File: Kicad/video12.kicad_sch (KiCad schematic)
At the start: 18 parts, among them J401 DE15HD, U401 THS7316, U402 TPD7S019

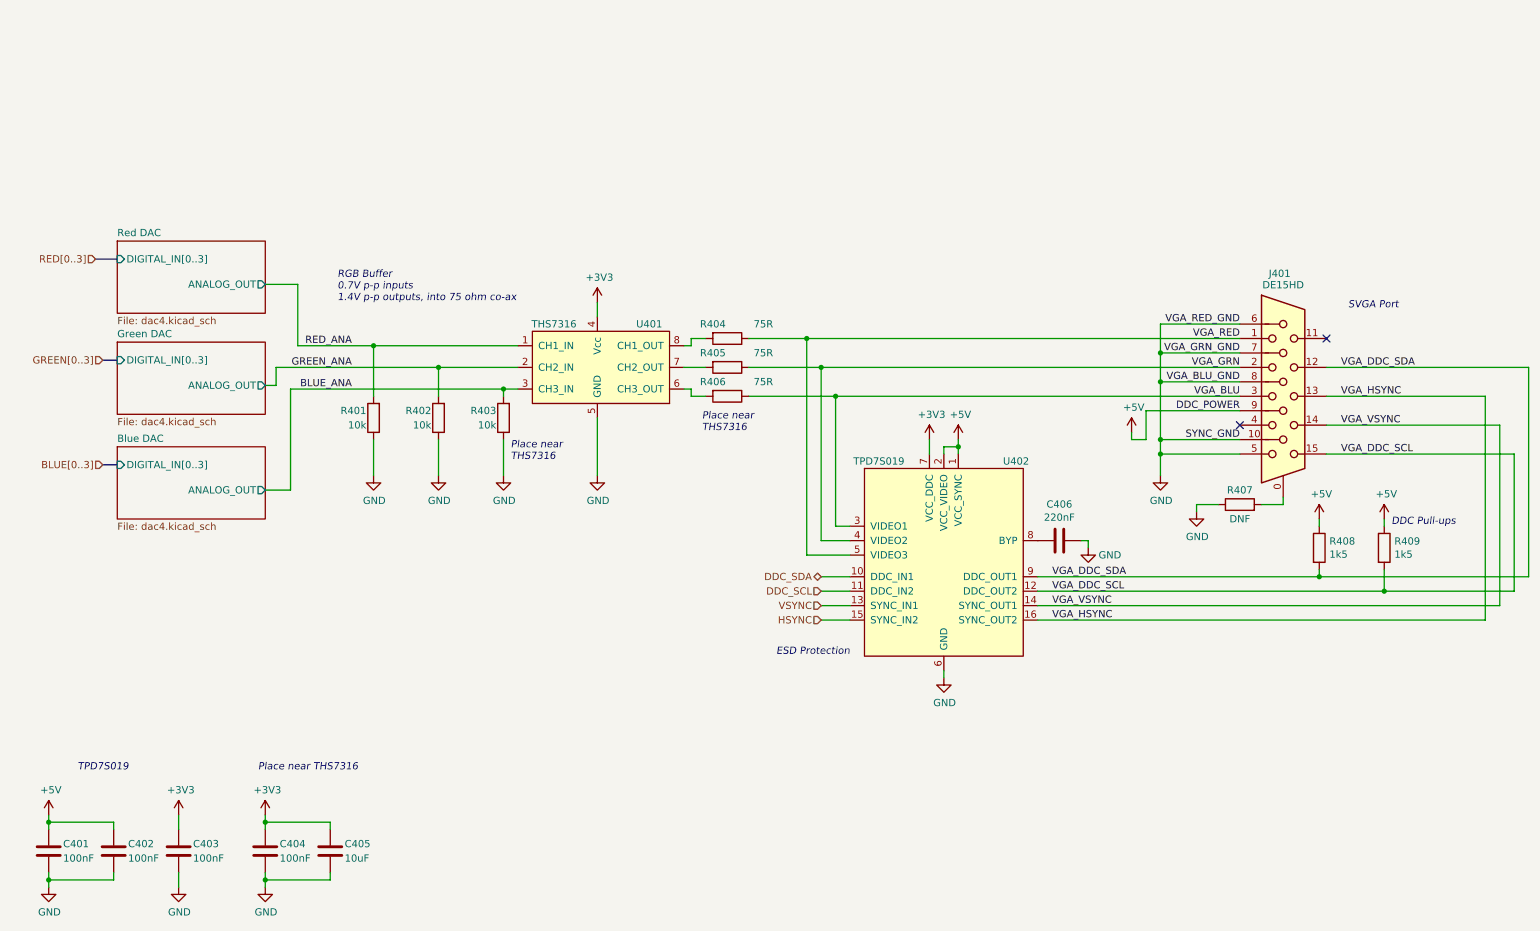
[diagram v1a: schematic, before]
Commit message: Retitle sheets and renumber parts.
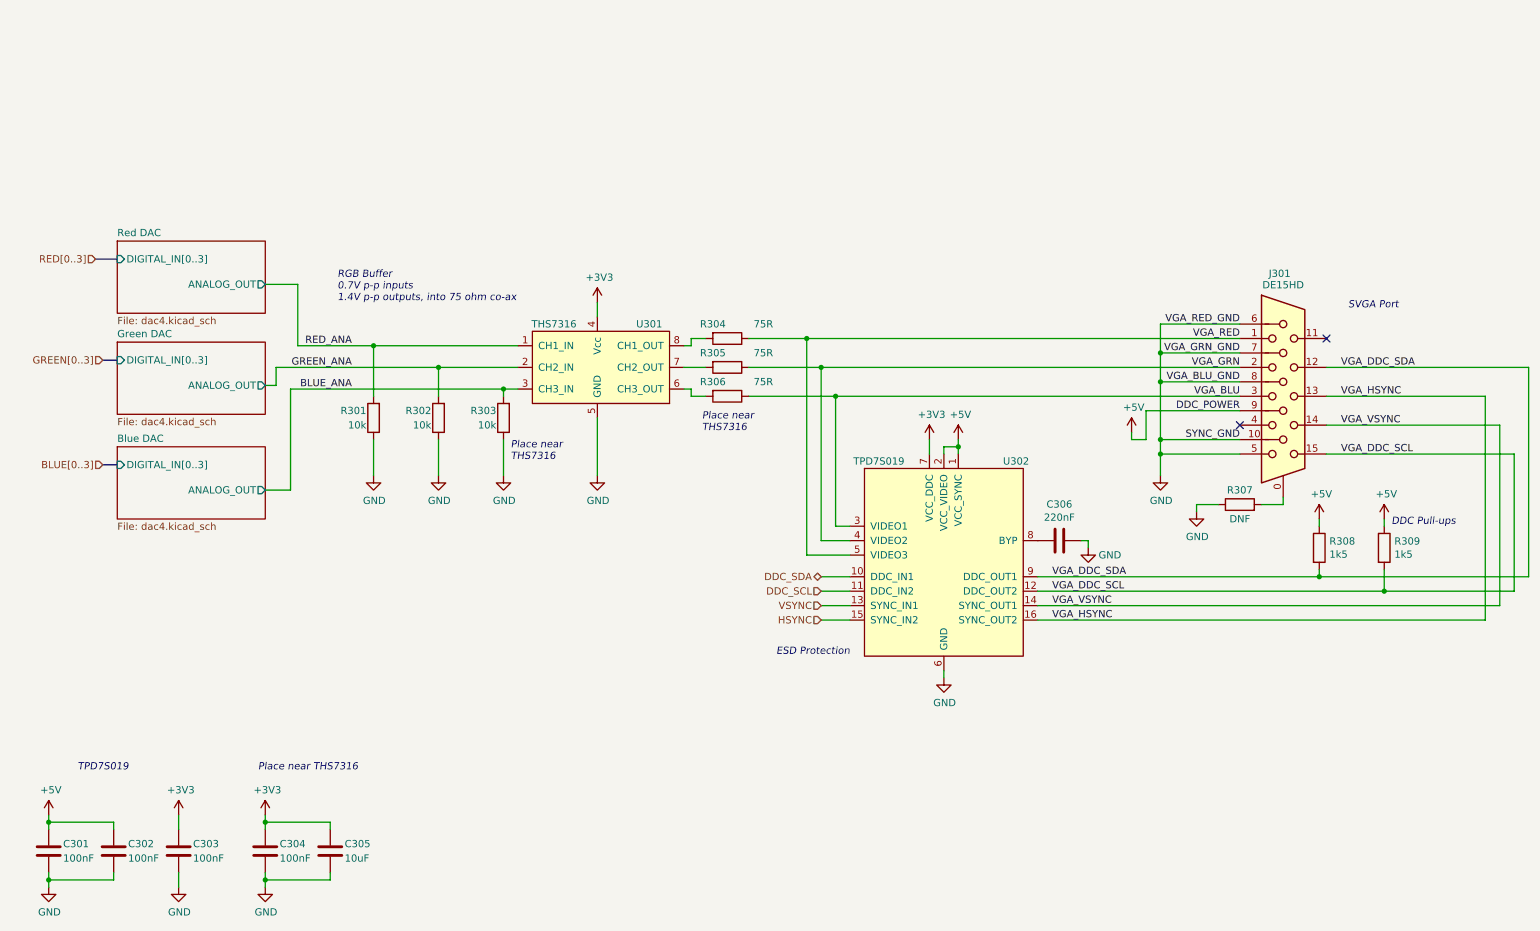
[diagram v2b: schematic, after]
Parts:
- renumbered C401 to C301, C402 to C302, C403 to C303, C404 to C304, C405 to C305, C406 to C306, J401 to J301, R401 to R301, R402 to R302, R403 to R303, R404 to R304, R405 to R305, R406 to R306, R407 to R307, R408 to R308, R409 to R309, U401 to U301, U402 to U302
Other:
- company: https://neotron-compute.github.io/ -> https://neotron-compute.github.io

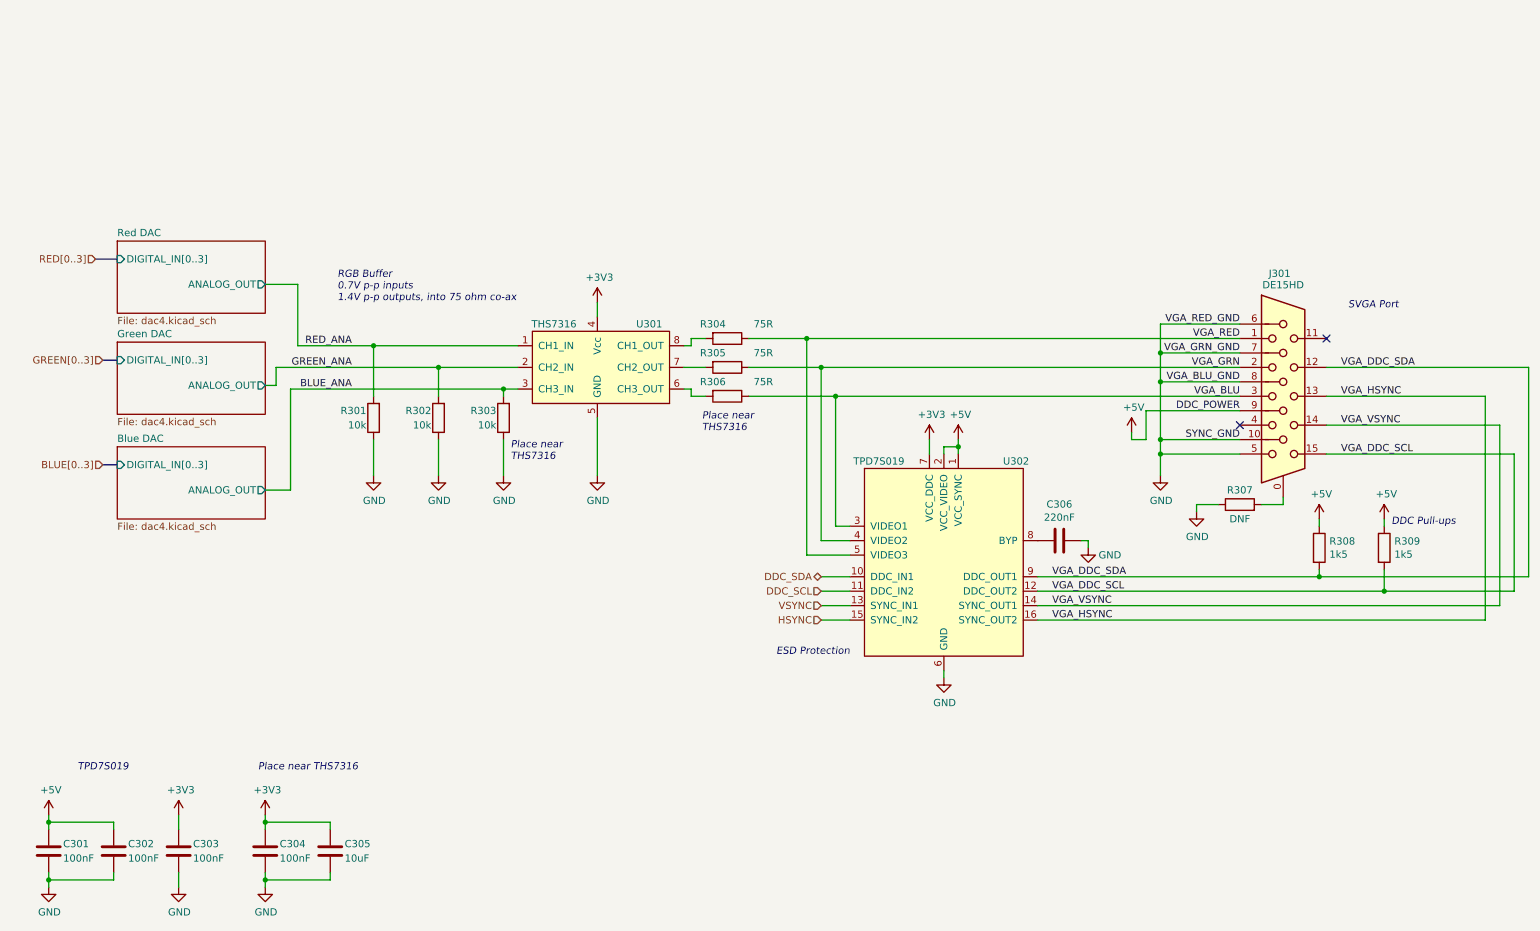
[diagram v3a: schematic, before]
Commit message: Set DAC to 1k/2k. Closes #77 Replaced some CPL resistors. Partial fix for #83 Added bridges for VGA I2C if ESD chip not fitted. Closes #51
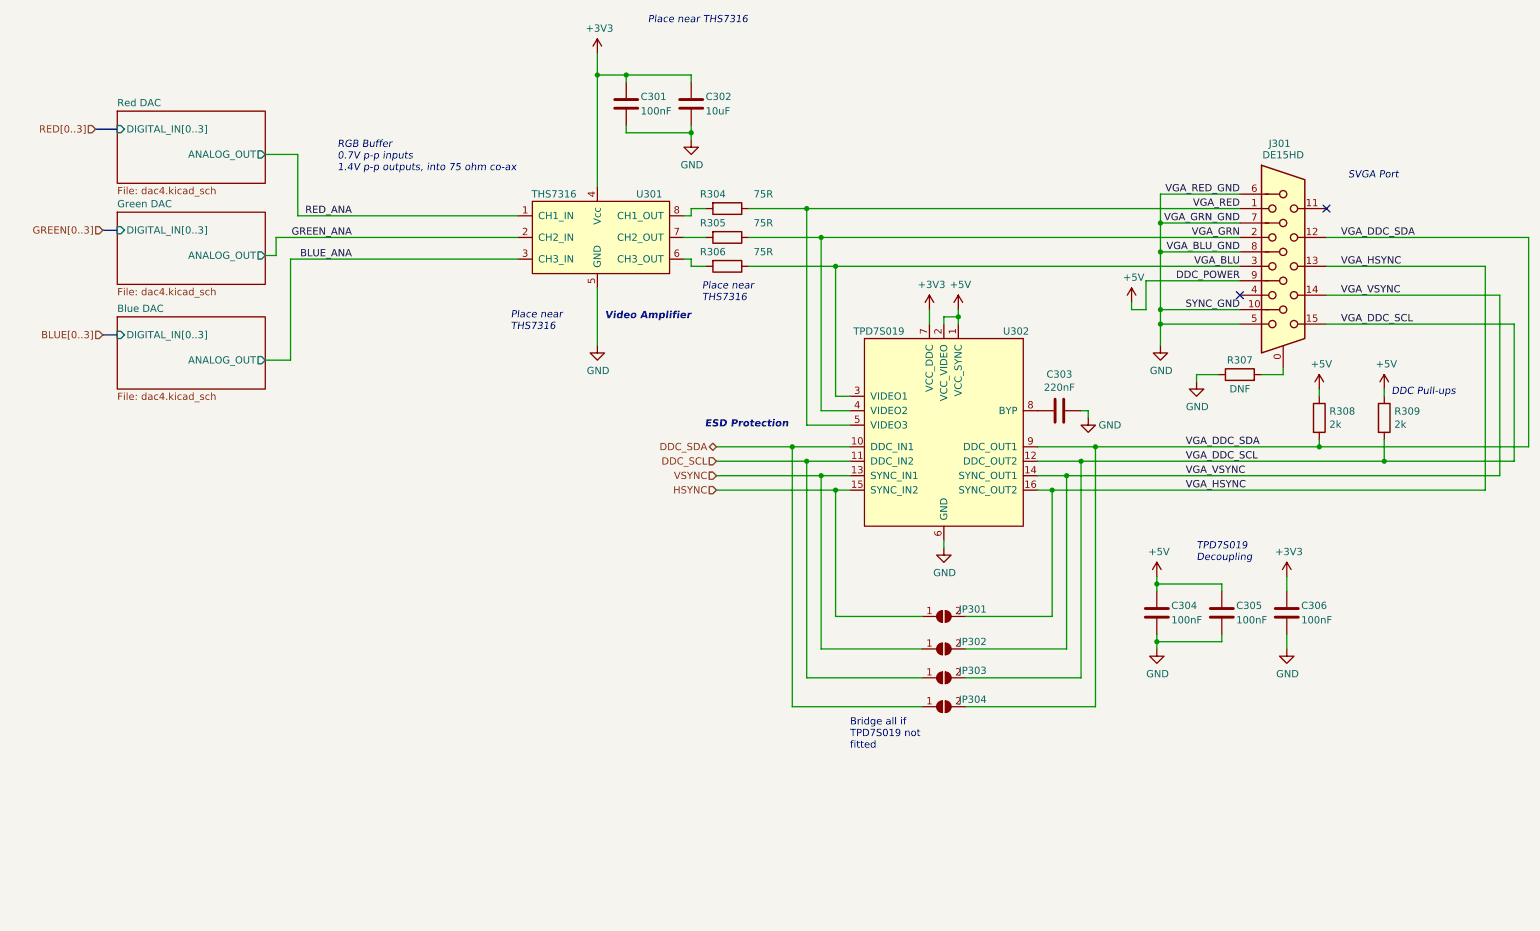
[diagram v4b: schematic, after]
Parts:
- removed R301, R302, R303: 10k, Resistor_SMD:R_0805_2012Metric_Pad1.20x1.40mm_HandSolder, symbol Device:R
- added JP301, JP302, JP303, JP304: Bridge, Jumper:SolderJumper-2_P1.3mm_Open_RoundedPad1.0x1.5mm, symbol Jumper:SolderJumper_2_Open
- R304, R305, R306: Digikey RMCF0805FT75R0-ND -> RMCF0805FT75R0CT-ND
- R308, R309: value 1k5 -> 2k; Digikey RMCF0805FT1K50-ND -> RMCF0805FT2K00CT-ND; LCSC Part# C4310 -> C17604; MPN RMCF0805FT1K50 -> RMCF0805FT2K00
- renumbered C304 to C301, C305 to C302, C306 to C303, C301 to C304, C302 to C305, C303 to C306
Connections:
- net DDC_SCL: now also JP303.1 (A)
- net DDC_SDA: now also JP304.1 (A)
- net HSYNC: now also JP301.1 (A)
- net VGA_DDC_SCL: now also JP303.2 (B)
- net VGA_DDC_SDA: now also JP304.2 (B)
- net VGA_HSYNC: now also JP301.2 (B)
- net VGA_VSYNC: now also JP302.2 (B)
- net VSYNC: now also JP302.1 (A)
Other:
- note added: "Bridge all if TPD7S019 not fitted"
- note added: "TPD7S019 Decoupling"
- note added: "Video Amplifier"
- note removed: "TPD7S019"
- moved on the sheet: C301, C302, C303, C304, C305, C306, J301, R304, R305, R306, R307, R308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

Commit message: Removed all CPL parts, and changed standby PSU.
The Holtek was a SOT-89 that had a completely different pinout to
every other SOT-89 3.3V LDO out there. To avoid confusion I
wanted to replace it, but the only other basic JLCPCB parts
were the AMS1117 (huge quiescent current) and something only
rated to 7V input voltage (this LDO gets the full VDC in).

So, I used a TO-92 footprint and picked an LP2950N.

This, however, needs some ESR on the output cap, so I made
that a 2.2uF electrolytic.

I also removed the 2x 10uF output caps on the K7805 and set
just one 22uF as specified in the datasheet.
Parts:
- C301, C304, C305, C306: Digikey (none) -> 399-C0805C104M5RAC7800CT-ND; MPN CPL-CAP-X7R-0805-100NF-50V -> C0805C104M5RACTU; Manufacturer CPL -> Kemet; Mouser (none) -> 80-C0805C104M5R
- C302: Digikey (none) -> 490-3886-1-ND; MPN CPL-CAP-X5R-0805-10UF-16V -> GRM21BR61C106KE15L; Manufacturer CPL -> Murata; Mouser (none) -> 81-GRM21BR61C106KE15
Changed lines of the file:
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@@
       (effects (font (size 1.27 1.27)) hide)
     )
-    (property "Digikey" "~" (id 5) (at 226.695 139.7 0)
-      (effects (font (size 1.27 1.27)) hide)
-    )
-    (property "MPN" "CPL-CAP-X7R-0805-100NF-50V" (id 6) (at 226.695 139.7 0)
-      (effects (font (size 1.27 1.27)) hide)
-    )
-    (property "Manufacturer" "CPL" (id 7) (at 226.695 139.7 0)
-      (effects (font (size 1.27 1.27)) hide)
-    )
-    (property "Mouser" "~" (id 8) (at 226.695 139.7 0)
+    (property "Digikey" "399-C0805C104M5RAC7800CT-ND" (id 5) (at 226.695 139.7 0)
+      (effects (font (size 1.27 1.27)) hide)
+    )
+    (property "MPN" "C0805C104M5RACTU" (id 6) (at 226.695 139.7 0)
+      (effects (font (size 1.27 1.27)) hide)
+    )
+    (property "Manufacturer" "Kemet" (id 7) (at 226.695 139.7 0)
+      (effects (font (size 1.27 1.27)) hide)
+    )
+    (property "Mouser" "80-C0805C104M5R" (id 8) (at 226.695 139.7 0)
       (effects (font (size 1.27 1.27)) hide)
     )
@@
       (effects (font (size 1.27 1.27)) hide)
     )
-    (property "Digikey" "~" (id 5) (at 121.92 50.165 0)
-      (effects (font (size 1.27 1.27)) hide)
-    )
-    (property "MPN" "CPL-CAP-X7R-0805-100NF-50V" (id 6) (at 121.92 50.165 0)
-      (effects (font (size 1.27 1.27)) hide)
-    )
-    (property "Manufacturer" "CPL" (id 7) (at 121.92 50.165 0)
-      (effects (font (size 1.27 1.27)) hide)
-    )
-    (property "Mouser" "~" (id 8) (at 121.92 50.165 0)
+    (property "Digikey" "399-C0805C104M5RAC7800CT-ND" (id 5) (at 121.92 50.165 0)
+      (effects (font (size 1.27 1.27)) hide)
+    )
+    (property "MPN" "C0805C104M5RACTU" (id 6) (at 121.92 50.165 0)
+      (effects (font (size 1.27 1.27)) hide)
+    )
+    (property "Manufacturer" "Kemet" (id 7) (at 121.92 50.165 0)
+      (effects (font (size 1.27 1.27)) hide)
+    )
+    (property "Mouser" "80-C0805C104M5R" (id 8) (at 121.92 50.165 0)
       (effects (font (size 1.27 1.27)) hide)
     )
@@
       (effects (font (size 1.27 1.27)) hide)
     )
-    (property "Digikey" "~" (id 5) (at 133.35 50.165 0)
-      (effects (font (size 1.27 1.27)) hide)
-    )
-    (property "MPN" "CPL-CAP-X5R-0805-10UF-16V" (id 6) (at 133.35 50.165 0)
-      (effects (font (size 1.27 1.27)) hide)
-    )
-    (property "Manufacturer" "CPL" (id 7) (at 133.35 50.165 0)
+    (property "Digikey" "490-3886-1-ND" (id 5) (at 133.35 50.165 0)
+      (effects (font (size 1.27 1.27)) hide)
+    )
+    (property "MPN" "GRM21BR61C106KE15L" (id 6) (at 133.35 50.165 0)
+      (effects (font (size 1.27 1.27)) hide)
+    )
+    (property "Manufacturer" "Murata" (id 7) (at 133.35 50.165 0)
       (effects (font (size 1.27 1.27)) hide)
     )
@@
       (effects (font (size 1.27 1.27)) hide)
     )
-    (property "Mouser" "~" (id 11) (at 133.35 50.165 0)
+    (property "Mouser" "81-GRM21BR61C106KE15" (id 11) (at 133.35 50.165 0)
       (effects (font (size 1.27 1.27)) hide)
     )
@@
       (effects (font (size 1.27 1.27)) hide)
     )
-    (property "Digikey" "~" (id 5) (at 215.265 139.7 0)
-      (effects (font (size 1.27 1.27)) hide)
-    )
-    (property "MPN" "CPL-CAP-X7R-0805-100NF-50V" (id 6) (at 215.265 139.7 0)
-      (effects (font (size 1.27 1.27)) hide)
-    )
-    (property "Manufacturer" "CPL" (id 7) (at 215.265 139.7 0)
-      (effects (font (size 1.27 1.27)) hide)
-    )
-    (property "Mouser" "~" (id 8) (at 215.265 139.7 0)
+    (property "Digikey" "399-C0805C104M5RAC7800CT-ND" (id 5) (at 215.265 139.7 0)
+      (effects (font (size 1.27 1.27)) hide)
+    )
+    (property "MPN" "C0805C104M5RACTU" (id 6) (at 215.265 139.7 0)
+      (effects (font (size 1.27 1.27)) hide)
+    )
+    (property "Manufacturer" "Kemet" (id 7) (at 215.265 139.7 0)
+      (effects (font (size 1.27 1.27)) hide)
+    )
+    (property "Mouser" "80-C0805C104M5R" (id 8) (at 215.265 139.7 0)
       (effects (font (size 1.27 1.27)) hide)
     )
@@
       (effects (font (size 1.27 1.27)) hide)
     )
-    (property "Digikey" "~" (id 5) (at 238.125 139.7 0)
-      (effects (font (size 1.27 1.27)) hide)
-    )
-    (property "MPN" "CPL-CAP-X7R-0805-100NF-50V" (id 6) (at 238.125 139.7 0)
-      (effects (font (size 1.27 1.27)) hide)
-    )
-    (property "Manufacturer" "CPL" (id 7) (at 238.125 139.7 0)
-      (effects (font (size 1.27 1.27)) hide)
-    )
-    (property "Mouser" "~" (id 8) (at 238.125 139.7 0)
-      (effects (font (size 1.27 1.27)) hide)
-    )
+    (property "Digikey" "399-C0805C104M5RAC7800CT-ND" (id 5) (at 238.125 139.7 0)
+      (effects (font (size 1.27 1.27)) hide)
+    )
+    (property "MPN" "C0805C104M5RACTU" (id 6) (at 238.125 139.7 0)
+      (effects (font (size 1.27 1.27)) hide)
+    )
+    (property "Manufacturer" "Kemet" (id 7) (at 238.125 139.7 0)
+      (effects (font (size 1.27 1.27)) hide)
+    )
+    (property "Mouser" "80-C0805C104M5R" (id 8) (at 238.125 139.7 0)
+      (effects (font (size 1.27 1.27)) hide)
+    )
